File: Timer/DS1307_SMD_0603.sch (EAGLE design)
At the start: 6 parts, among them Q1 32.768kHz, U1 DS1307Z

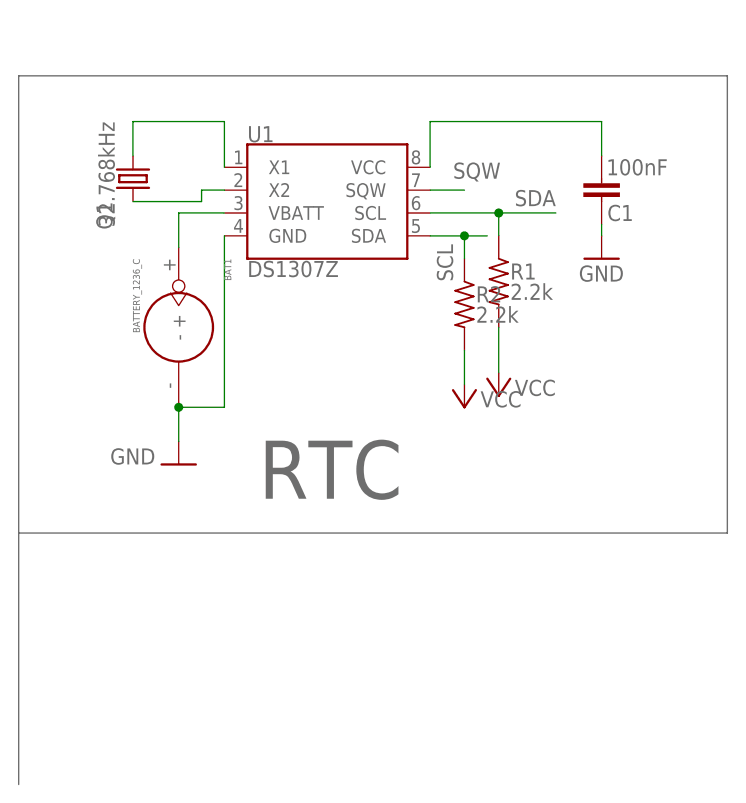
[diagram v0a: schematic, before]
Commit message: rtc smd updated
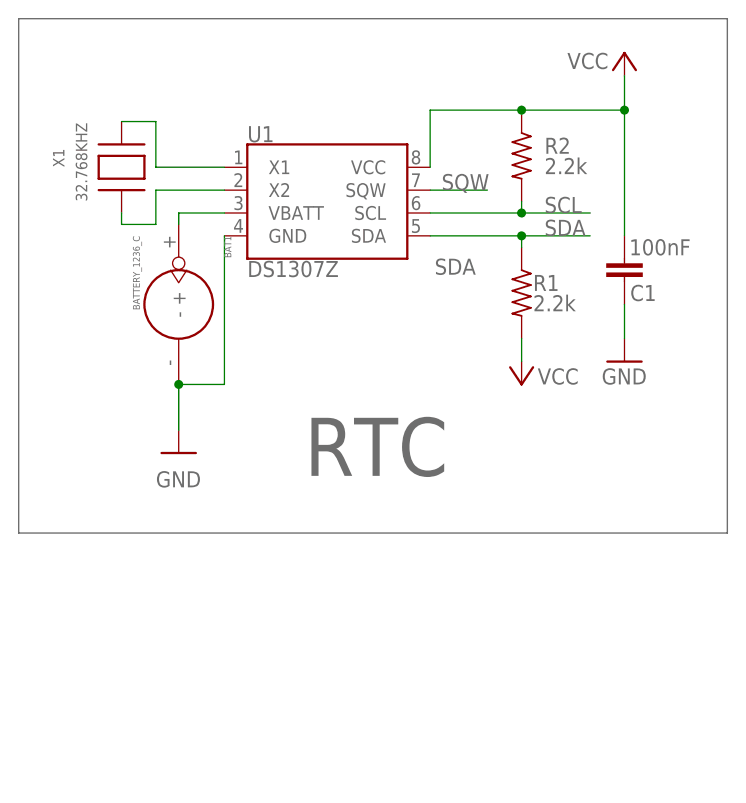
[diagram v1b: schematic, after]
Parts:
- removed Q1: 32.768kHz, SparkFun-Clocks:CRYSTAL-32.768KHZSMD-3.2X1.5
- added X1: 32.768KHZ, adafruit:XTAL-3.2X1.5
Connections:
- removed net N$3: C1.2, U1.VCC
- net N$1: now also X1.P$2; no longer Q1.1
- net N$2: now also X1.P$1; no longer Q1.2
- net SCL: now also R2.2, U1.SCL; no longer R2.1, U1.SDA
- net SDA: now also U1.SDA; no longer U1.SCL
- net VCC: now also C1.2, R2.1, U1.VCC; no longer R2.2
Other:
- moved on the sheet: BAT1, C1, R1, R2
